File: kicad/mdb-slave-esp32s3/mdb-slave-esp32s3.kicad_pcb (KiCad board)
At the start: 2 copper layers, 39 x 40 mm, 45 parts, among them J1 MDB_Connector, J2 USB_C_Receptacle_USB2.0_16P, J3 Conn_01x03_Pin, J8 Conn_01x04_Pin, Q7 MMBT3904, SW1 SW_Push, U1 TLP785, U3 ESP32-S3FH4R2, U4 TLP785, U5 LM2594HVM-3.3, Y1 Crystal_GND24

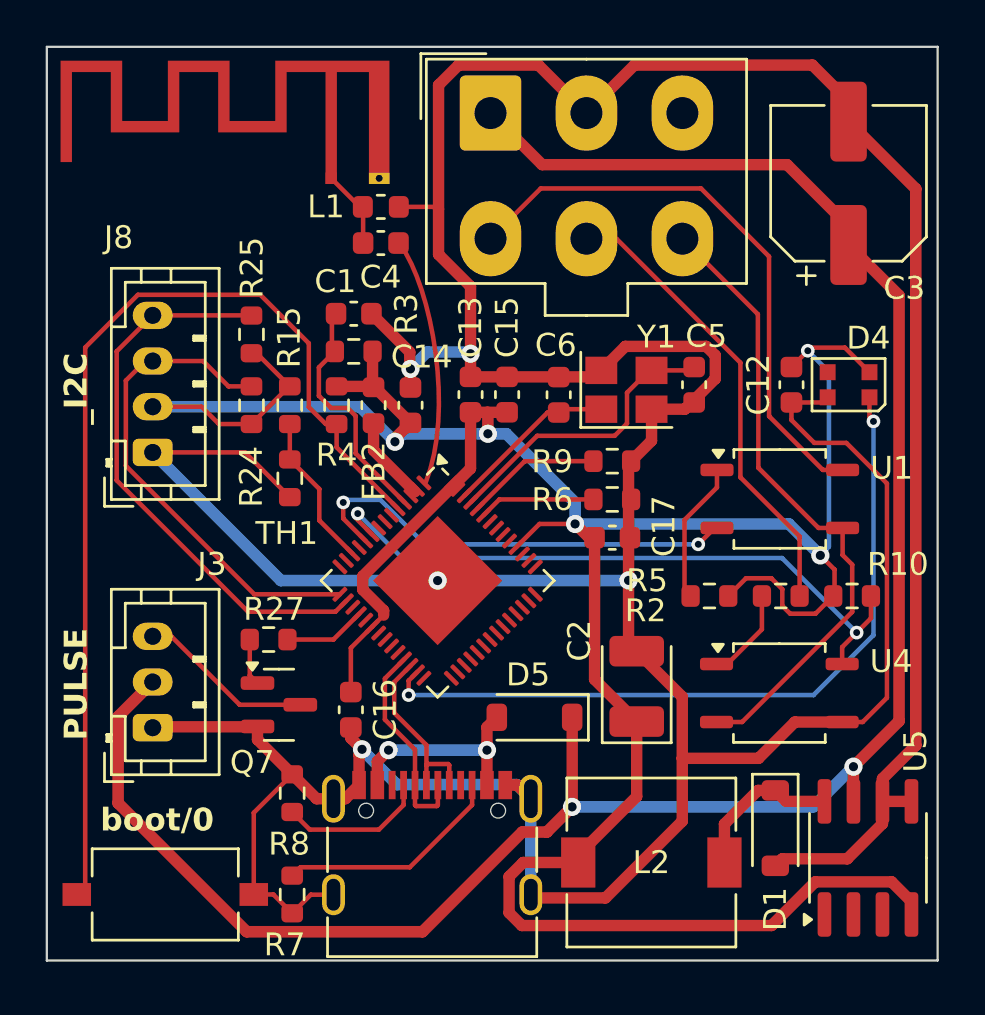
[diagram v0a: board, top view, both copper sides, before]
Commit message: Updating PCBway rules
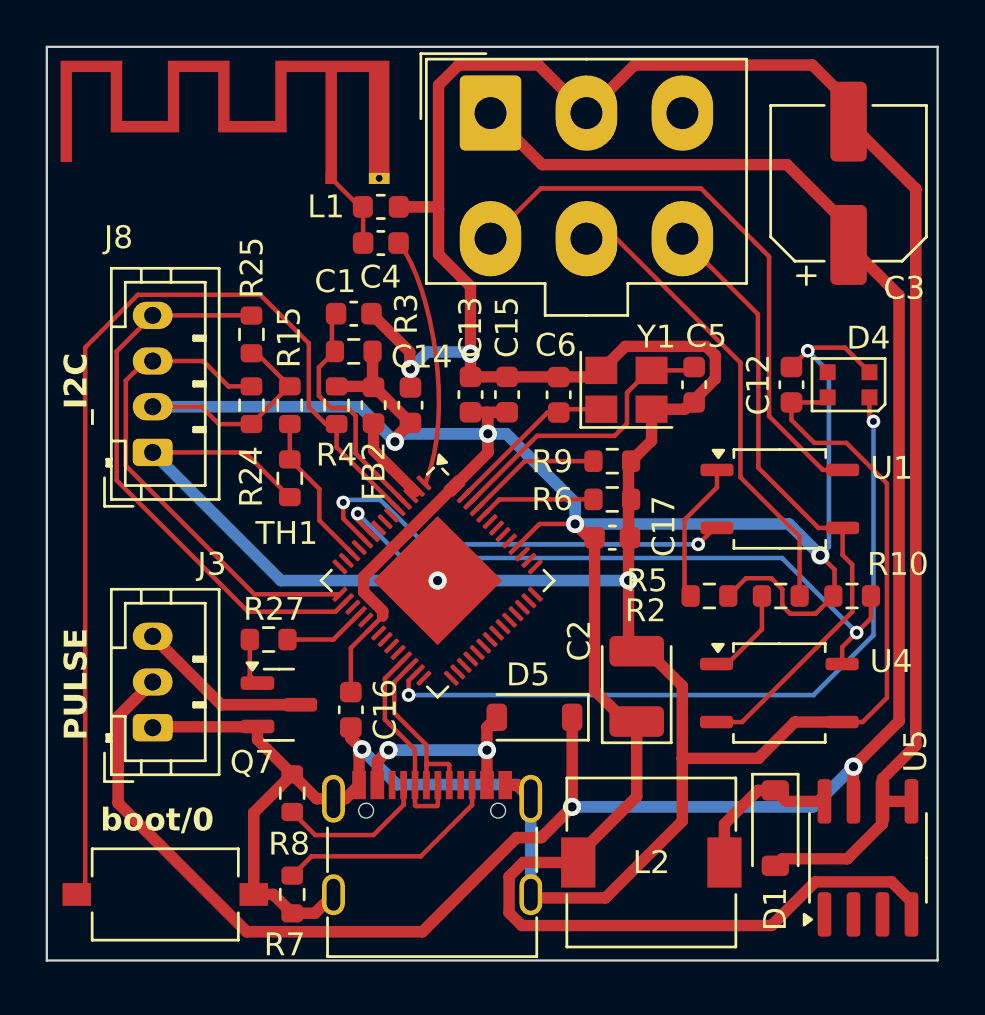
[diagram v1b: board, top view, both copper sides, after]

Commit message: PCBway rules
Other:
- board text added: "_i2C"
- board text removed: "_I2C"

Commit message: routing...
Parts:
- moved D1 0.61 mm to (200.4, 116.7)
- moved L2 0.61 mm to (195.0, 118.2)
- moved C15 0.56 mm to (189.2, 98.3)
- moved U4 0.45 mm to (200.6, 110.9)
- moved C13 0.37 mm to (187.4, 98.3)
- moved R10 0.23 mm to (203.8, 106.9)
- moved R2 0.23 mm to (200.6, 106.9)
- moved R5 0.23 mm to (197.5, 106.9)
- moved C14 0.07 mm to (184.5, 98.8)
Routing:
- net GND: track 221.3 -> 89.0 mm, vias 5 -> 8
- net /vin: track 92.0 -> 79.1 mm, vias 2 -> 1
- net +3V3: track 132.6 -> 125.3 mm
- net /io4: track 28.8 -> 28.0 mm
- net /mdb_communications_common: track 28.0 -> 27.3 mm
- net Net-(R2-Pad2): track 4.08 -> 3.58 mm
- added copper zone on B.Cu, net GND

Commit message: Routing...
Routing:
- net GND: track 89.0 -> 100.0 mm, vias 8 -> 6

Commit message: routing...
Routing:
- net GND: track 100.0 -> 99.1 mm

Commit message: Routing
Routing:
- net GND: track 99.1 -> 71.4 mm, vias 6 -> 10
- net /io21: track 33.0 -> 32.0 mm

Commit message: commit: xxxxxxx
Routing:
- net GND: track 71.4 -> 68.9 mm
- net /io21: track 32.0 -> 34.3 mm
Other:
- board text added: "commit: xxxxxxx"

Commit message: routing
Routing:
- net GND: track 68.9 -> 94.4 mm, vias 10 -> 8
